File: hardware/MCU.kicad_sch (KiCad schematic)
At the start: 22 parts, among them Q1 2N2219, Q2 2N2219, SW2 GPIO_N_RST, SW3 SW_SYS-PWR, SW4 GPIO_HW_ADDR_SEL, U3 SX1509BIULTRT

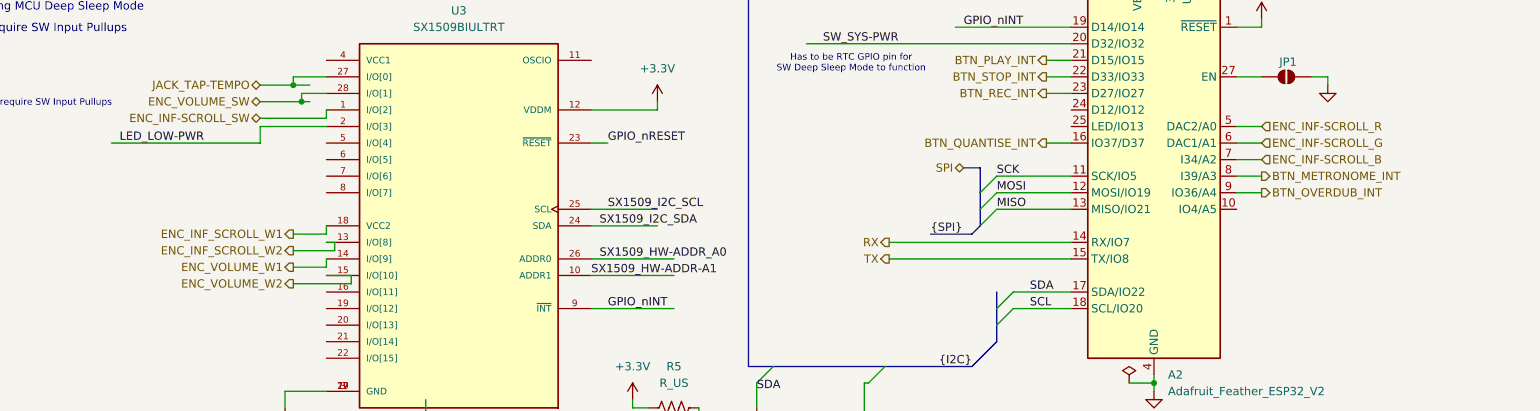
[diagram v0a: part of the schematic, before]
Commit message: fix [HWE]: Reassigned Rot Enc outs to new MCU GPIO
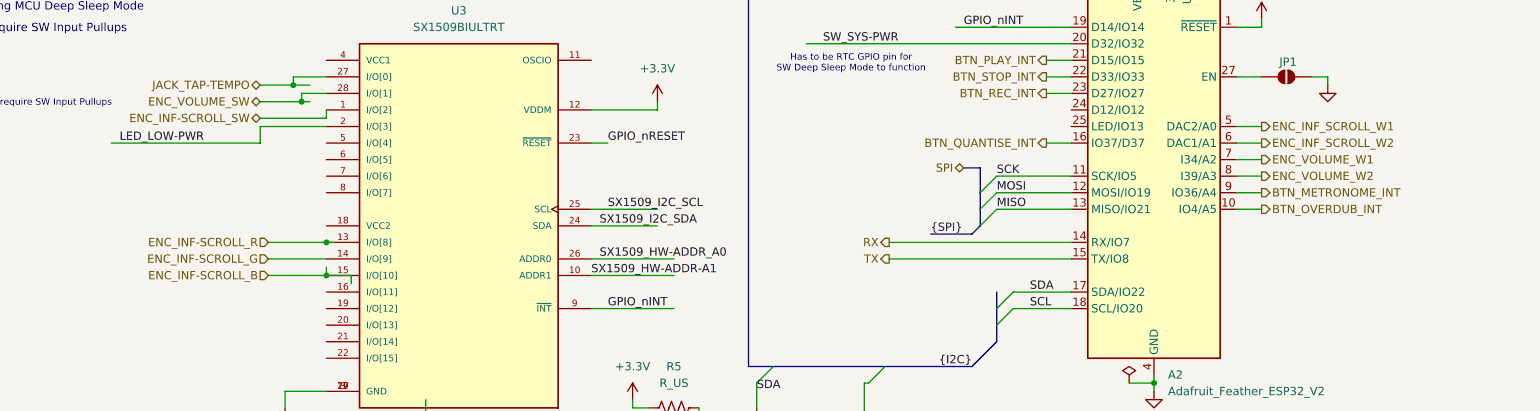
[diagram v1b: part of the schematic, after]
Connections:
- net BTN_METRONOME_INT: now also A2.9 (IO36/A4); no longer A2.8 (I39/A3)
- net BTN_OVERDUB_INT: now also A2.10 (IO4/A5); no longer A2.9 (IO36/A4)
- net ENC_INF-SCROLL_B: now also U3.15 (I/O[10]); no longer A2.7 (I34/A2)
- net ENC_INF-SCROLL_G: now also U3.14 (I/O[9]); no longer A2.6 (DAC1/A1)
- net ENC_INF-SCROLL_R: now also U3.13 (I/O[8]); no longer A2.5 (DAC2/A0)
- net ENC_INF_SCROLL_W1: now also A2.5 (DAC2/A0); no longer U3.18 (VCC2)
- net ENC_INF_SCROLL_W2: now also A2.6 (DAC1/A1); no longer U3.13 (I/O[8])
- net ENC_VOLUME_W1: now also A2.7 (I34/A2); no longer U3.14 (I/O[9])
- net ENC_VOLUME_W2: now also A2.8 (I39/A3); no longer U3.15 (I/O[10])

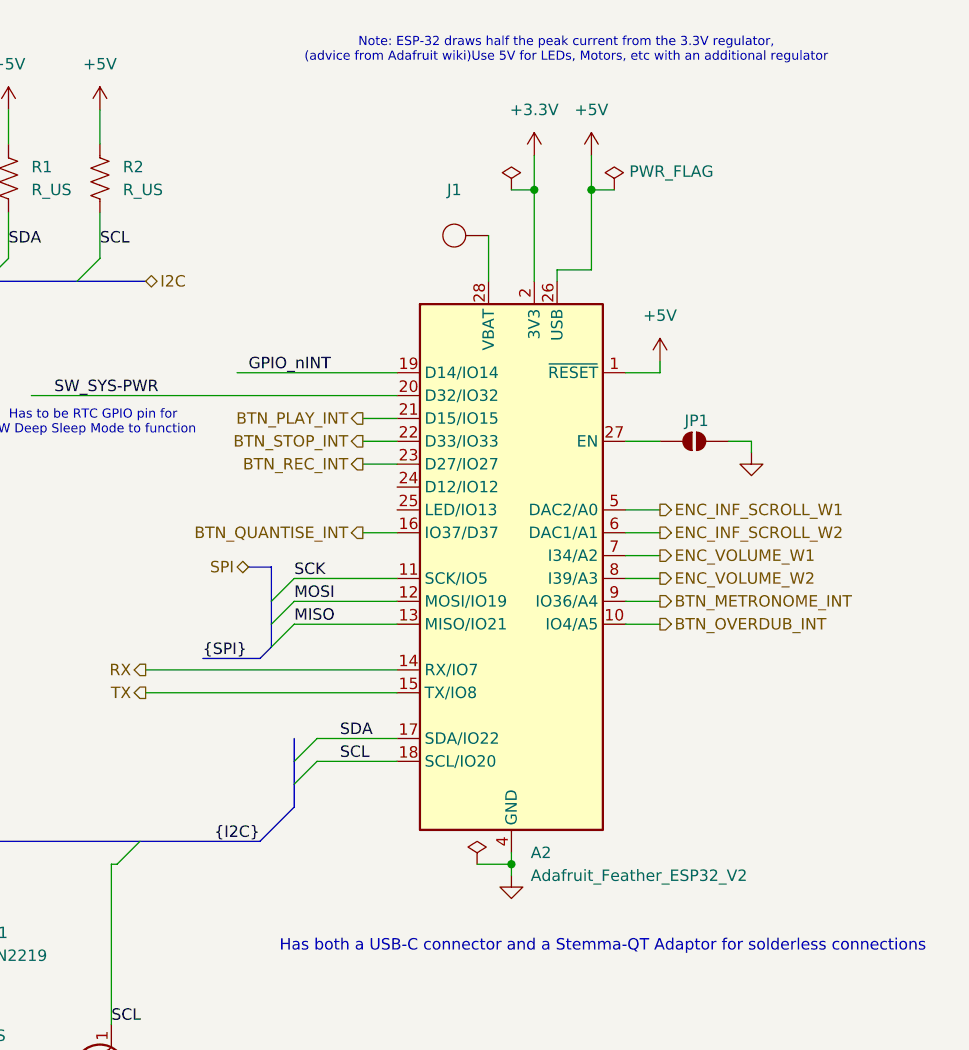
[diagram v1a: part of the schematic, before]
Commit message: feat![HWE]: Changed MCU to Adafruit ESP32-S3
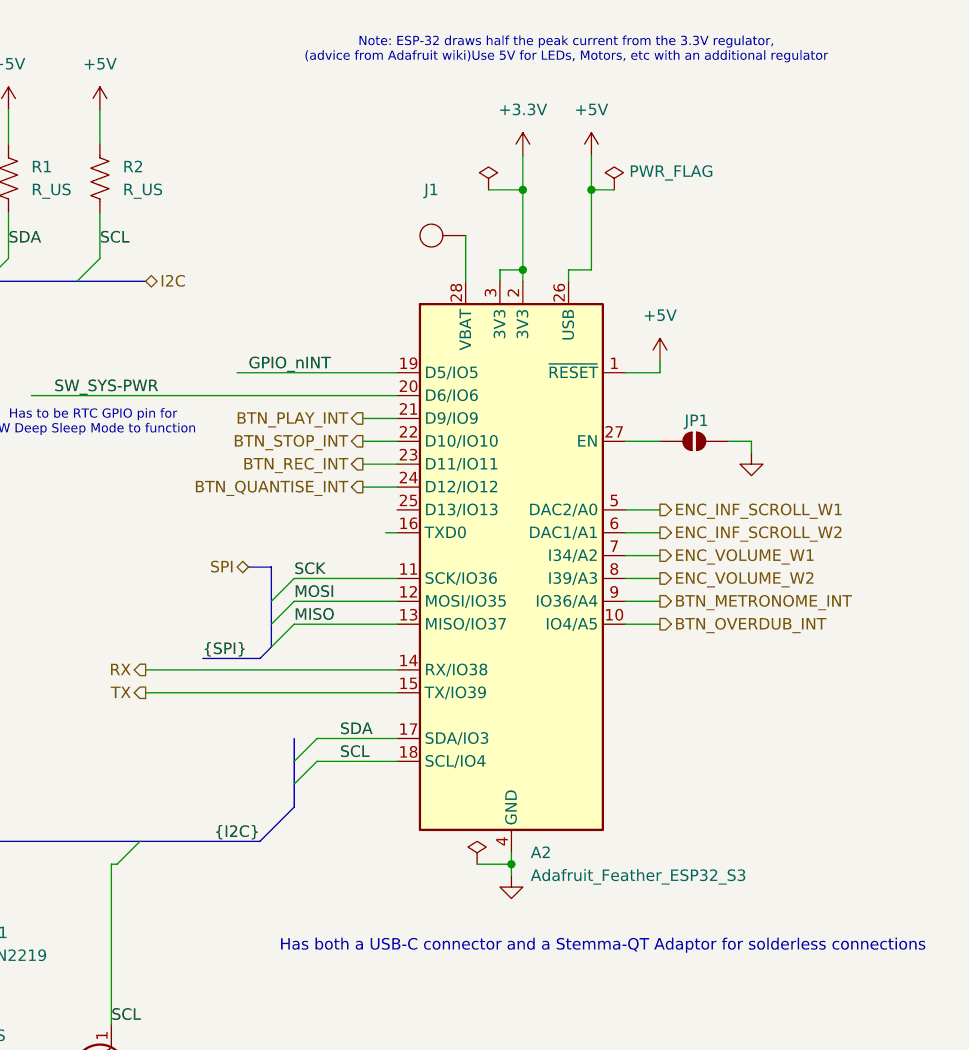
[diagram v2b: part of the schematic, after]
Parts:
- A2: value Adafruit_Feather_ESP32_V2 -> Adafruit_Feather_ESP32_S3; footprint Adafruit_Feather_ESP32_V2:Adafruit_Feather_ESP32_V2_WithMountingHoles -> Adafruit_Feather_ESP32_S3_with_headers:Adafruit_Feather_ESP32_S3_WithMountingHoles; symbol Adafruit_Feather_ESP32_V2:Adafruit_Feather_ESP32_V2 -> Adafruit_Feather_ESP32_S3:Adafruit_Feather_ESP32_S3; now in the parts list
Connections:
- net +3.3V: now also A2.3 (3V3)
- net BTN_QUANTISE_INT: now also A2.24 (D12/IO12); no longer A2.16 (IO37/D37)
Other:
- company: (none) -> Madueke Systems and Technologies
- title: (none) -> Simple Midi Transport Controller
- moved on the sheet: J1
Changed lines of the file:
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@@
 	(generator_version "9.0")
 	(paper "A4")
+	(title_block
+		(title "Simple Midi Transport Controller")
+		(date "2026-04-06")
+		(rev "1")
+		(company "Madueke Systems and Technologies")
+		(comment 1 "Used the combination of the Adafruit Feather ESP32-V2 Dev Board and the SX1509 IO expander")
+	)
 	(bus_alias "I2C"
 		(members "SDA" "SCL")
@@
 	)
 	(junction
+		(at 207.01 33.02)
+		(diameter 0)
+		(color 0 0 0 0)
+	)
+	(junction
 		(at 78.74 86.36)
 		(diameter 0)
@@
 	)
 	(junction
-		(at 208.28 33.02)
+		(at 139.7 167.64)
 		(diameter 0)
 		(color 0 0 0 0)
 	)
 	(junction
-		(at 139.7 167.64)
+		(at 104.14 173.99)
 		(diameter 0)
 		(color 0 0 0 0)
 	)
 	(junction
-		(at 104.14 173.99)
+		(at 134.62 167.64)
 		(diameter 0)
 		(color 0 0 0 0)
 	)
 	(junction
-		(at 134.62 167.64)
+		(at 207.01 41.91)
 		(diameter 0)
 		(color 0 0 0 0)
@@
 	(wire
 		(pts
+			(xy 204.47 43.18) (xy 204.47 41.91)
+		)
+		(stroke
+			(width 0)
+			(type default)
+		)
+	)
+	(wire
+		(pts
 			(xy 184.15 93.98) (xy 193.04 93.98)
 		)
@@
 	(wire
 		(pts
+			(xy 204.47 41.91) (xy 207.01 41.91)
+		)
+		(stroke
+			(width 0)
+			(type default)
+		)
+	)
+	(wire
+		(pts
 			(xy 45.72 71.12) (xy 68.58 71.12)
 		)
@@
 	(wire
 		(pts
+			(xy 191.77 71.12) (xy 193.04 71.12)
+		)
+		(stroke
+			(width 0)
+			(type default)
+		)
+	)
+	(wire
+		(pts
 			(xy 181.61 78.74) (xy 193.04 78.74)
 		)
@@
 	(wire
 		(pts
+			(xy 207.01 41.91) (xy 207.01 43.18)
+		)
+		(stroke
+			(width 0)
+			(type default)
+		)
+	)
+	(wire
+		(pts
 			(xy 201.93 107.95) (xy 205.74 107.95)
 		)
@@
 	(wire
 		(pts
-			(xy 210.82 41.91) (xy 210.82 43.18)
+			(xy 212.09 41.91) (xy 212.09 43.18)
 		)
 		(stroke
@@
 	(wire
 		(pts
-			(xy 205.74 33.02) (xy 208.28 33.02)
+			(xy 189.23 66.04) (xy 193.04 66.04)
+		)
+		(stroke
+			(width 0)
+			(type default)
+		)
+	)
+	(wire
+		(pts
+			(xy 203.2 33.02) (xy 207.01 33.02)
 		)
 		(stroke
@@
 	(wire
 		(pts
-			(xy 208.28 33.02) (xy 208.28 43.18)
+			(xy 207.01 33.02) (xy 207.01 41.91)
 		)
 		(stroke
@@
 	(wire
 		(pts
-			(xy 189.23 71.12) (xy 193.04 71.12)
-		)
-		(stroke
-			(width 0)
-			(type default)
-		)
-	)
-	(wire
-		(pts
-			(xy 208.28 29.21) (xy 208.28 33.02)
+			(xy 207.01 29.21) (xy 207.01 33.02)
 		)
 		(stroke
@@
 	(wire
 		(pts
-			(xy 214.63 41.91) (xy 210.82 41.91)
+			(xy 214.63 41.91) (xy 212.09 41.91)
 		)
 		(stroke
@@
 	(wire
 		(pts
-			(xy 203.2 38.1) (xy 203.2 43.18)
+			(xy 200.66 38.1) (xy 200.66 43.18)
 		)
 		(stroke
@@
 	(hierarchical_label "BTN_QUANTISE_INT"
 		(shape output)
-		(at 189.23 71.12 180)
+		(at 189.23 66.04 180)
 		(effects
 			(font
@@
 	)
 	(symbol
-		(lib_id "Adafruit_Feather_ESP32_V2:Adafruit_Feather_ESP32_V2")
+		(lib_id "Adafruit_Feather_ESP32_S3:Adafruit_Feather_ESP32_S3")
 		(at 205.74 73.66 0)
 		(unit 1)
 		(exclude_from_sim no)
-		(in_bom no)
+		(in_bom yes)
 		(on_board yes)
 		(dnp no)
@@
 			)
 		)
-		(property "Value" "Adafruit_Feather_ESP32_V2"
+		(property "Value" "Adafruit_Feather_ESP32_S3"
 			(at 207.8833 109.22 0)
 			(effects
@@
 			)
 		)
-		(property "Footprint" "Adafruit_Feather_ESP32_V2:Adafruit_Feather_ESP32_V2_WithMountingHoles"
+		(property "Footprint" "Adafruit_Feather_ESP32_S3_with_headers:Adafruit_Feather_ESP32_S3_WithMountingHoles"
 			(at 208.28 107.95 0)
 			(effects
@@
 			)
 		)
-		(property "Datasheet" "https://cdn-learn.adafruit.com/downloads/pdf/adafruit-esp32-feather-v2.pdf"
+		(property "Datasheet" "https://cdn-learn.adafruit.com/downloads/pdf/adafruit-esp32-s3-feather.pdf"
 			(at 205.74 104.14 0)
 			(effects
@@
 			)
 		)
-		(property "Description" "Microcontroller module with ESP32 MCU"
+		(property "Description" "Microcontroller Dev Kit  module with ESP32-S3 MCU and QT Qwiic Connector"
 			(at 205.74 73.66 0)
 			(effects
@@
 	(symbol
 		(lib_id "4ms_Power-symbol:+3.3V")
-		(at 208.28 29.21 0)
+		(at 207.01 29.21 0)
 		(unit 1)
 		(exclude_from_sim no)
@@
 		(fields_autoplaced yes)
 		(property "Reference" "#PWR01"
-			(at 208.28 33.02 0)
+			(at 207.01 33.02 0)
 			(effects
 				(font
@@
 		)
 		(property "Value" "+3.3V"
-			(at 208.28 24.13 0)
+			(at 207.01 24.13 0)
 			(effects
 				(font
@@
 		)
 		(property "Footprint" ""
-			(at 208.28 29.21 0)
+			(at 207.01 29.21 0)
 			(effects
 				(font
@@
 		)
 		(property "Datasheet" ""
-			(at 208.28 29.21 0)
+			(at 207.01 29.21 0)
 			(effects
 				(font
@@
 		)
 		(property "Description" ""
-			(at 208.28 29.21 0)
+			(at 207.01 29.21 0)
 			(effects
 				(font
@@
 	(symbol
 		(lib_id "power:PWR_FLAG")
-		(at 205.74 33.02 0)
+		(at 203.2 33.02 0)
 		(unit 1)
 		(exclude_from_sim no)
@@
 		(fields_autoplaced yes)
 		(property "Reference" "#FLG01"
-			(at 205.74 31.115 0)
+			(at 203.2 31.115 0)
 			(effects
 				(font
@@
 		)
 		(property "Value" "PWR_FLAG"
-			(at 205.74 27.94 0)
+			(at 203.2 27.94 0)
 			(effects
 				(font
@@
 		)
 		(property "Footprint" ""
-			(at 205.74 33.02 0)
+			(at 203.2 33.02 0)
 			(effects
 				(font
@@
 		)
 		(property "Datasheet" "~"
-			(at 205.74 33.02 0)
+			(at 203.2 33.02 0)
 			(effects
 				(font
@@
 		)
 		(property "Description" "Special symbol for telling ERC where power comes from"
-			(at 205.74 33.02 0)
+			(at 203.2 33.02 0)
 			(effects
 				(font
@@
 	(symbol
 		(lib_id "4ms_Connector:CAPSENSE_PAD")
-		(at 199.39 38.1 180)
+		(at 196.85 38.1 180)
 		(unit 1)
 		(exclude_from_sim no)
@@
 		(fields_autoplaced yes)
 		(property "Reference" "J1"
-			(at 199.39 33.02 0)
+			(at 196.85 33.02 0)
 			(effects
 				(font
@@
 		)
 		(property "Value" "~"
-			(at 199.39 35.56 0)
+			(at 196.85 35.56 0)
 			(effects
 				(font
@@
 		)
 		(property "Footprint" "4ms_Connector:CAPSENSE_PAD"
-			(at 189.484 33.02 0)
+			(at 186.944 33.02 0)
 			(effects
 				(font
@@
 		)
 		(property "Datasheet" ""
-			(at 199.39 38.1 0)
+			(at 196.85 38.1 0)
 			(effects
 				(font
@@
 		)
 		(property "Description" ""
-			(at 199.39 38.1 0)
+			(at 196.85 38.1 0)
 			(effects
 				(font

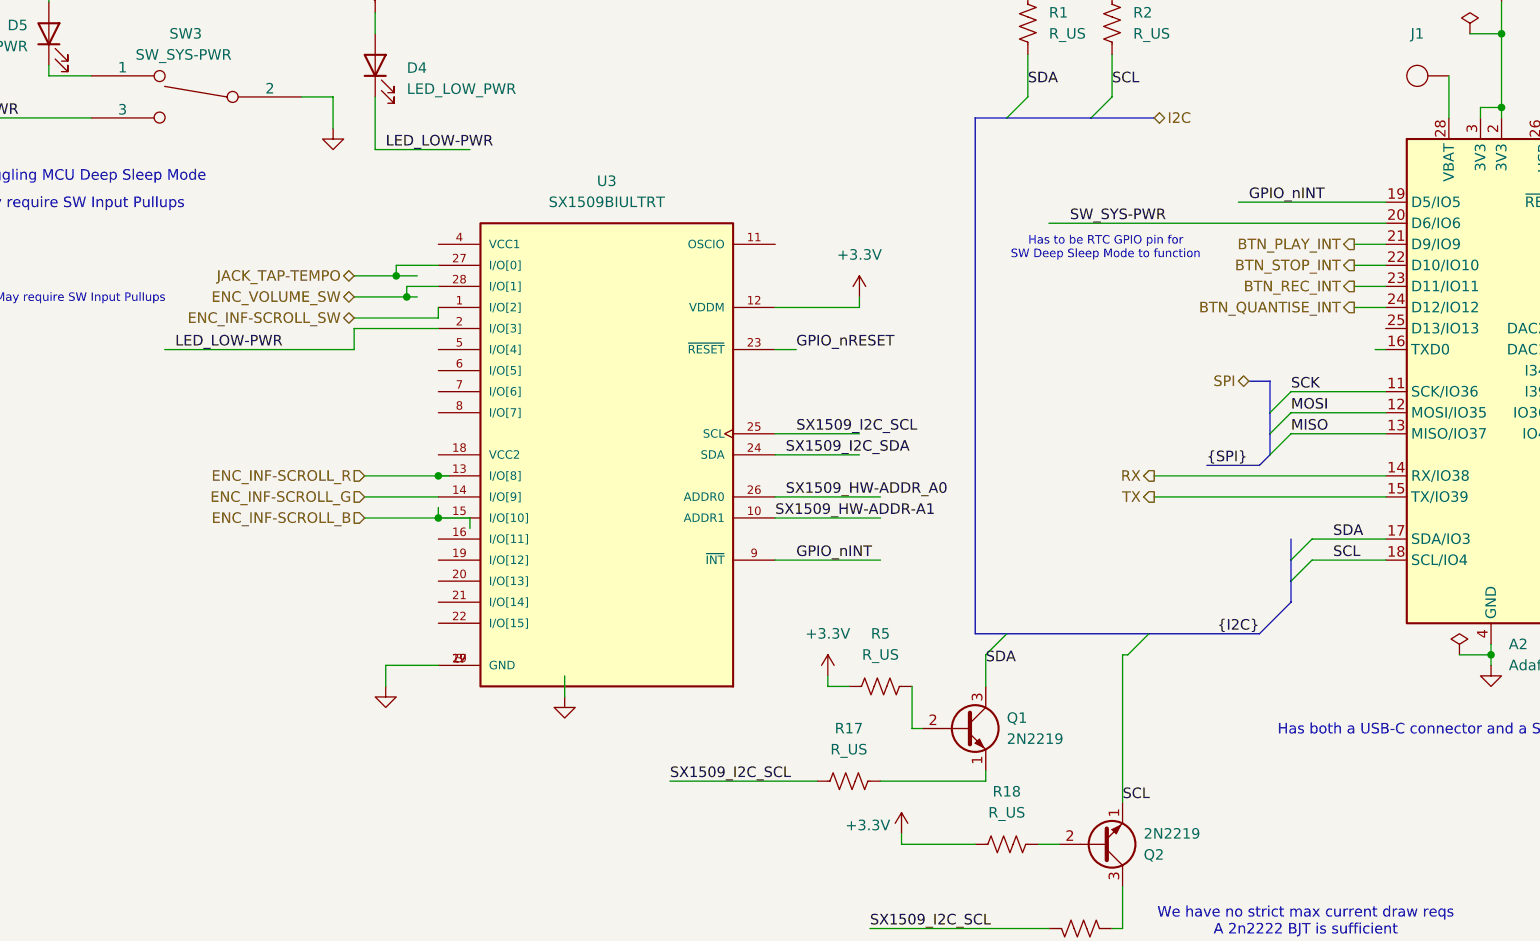
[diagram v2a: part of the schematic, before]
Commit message: fix [HWE]: Place DNPs for unused Pins
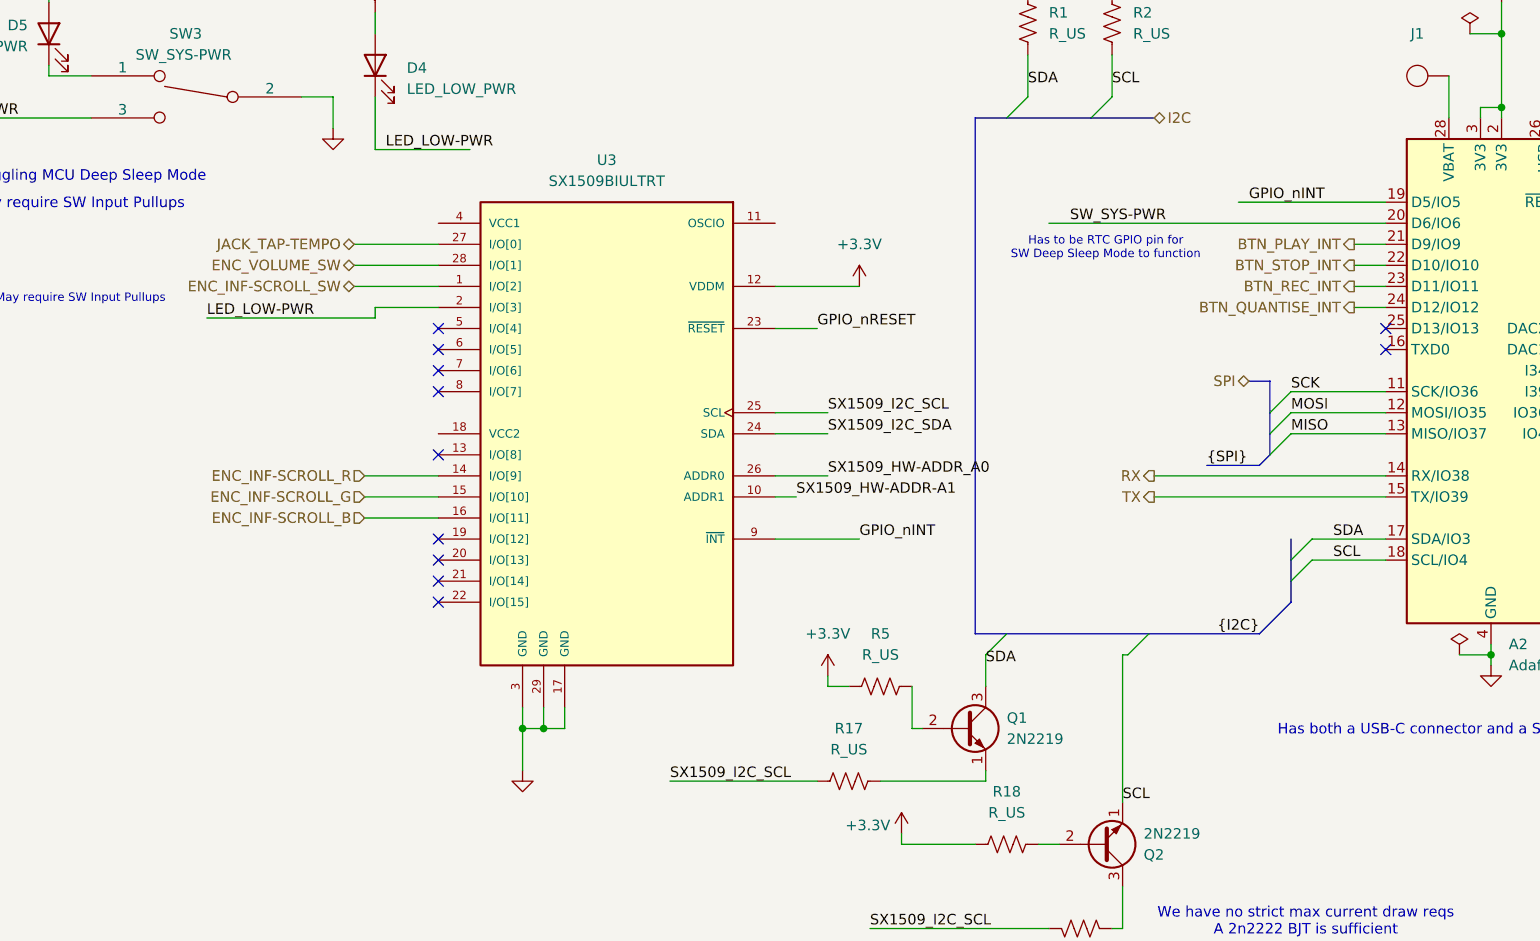
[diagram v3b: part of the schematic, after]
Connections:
- net ENC_INF-SCROLL_B: now also U3.16 (I/O[11]); no longer U3.15 (I/O[10])
- net ENC_INF-SCROLL_G: now also U3.15 (I/O[10]); no longer U3.14 (I/O[9])
- net ENC_INF-SCROLL_R: now also U3.14 (I/O[9]); no longer U3.13 (I/O[8])
- no-connect marks 0 -> 11
